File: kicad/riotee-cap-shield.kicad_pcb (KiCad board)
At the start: 2 copper layers, 55.9 x 22.9 mm, 11 parts, among them J1 Conn_01x12, J2 Conn_01x10, SW1 SW_DIP_x08

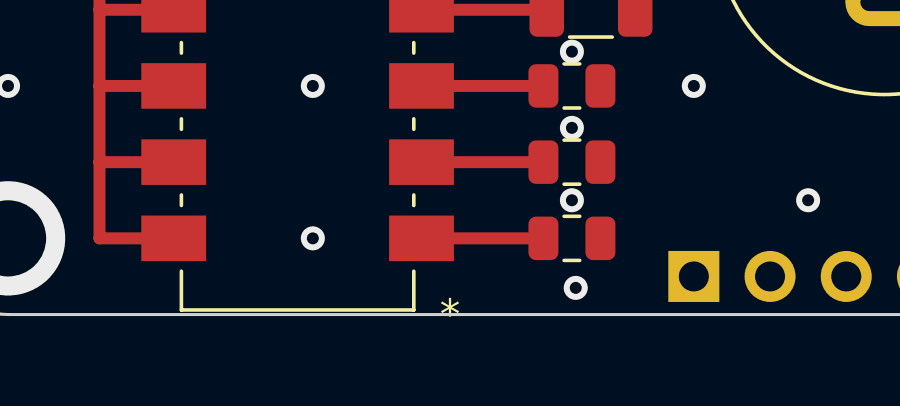
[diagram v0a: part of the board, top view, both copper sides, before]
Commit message: add MPNs in schematics
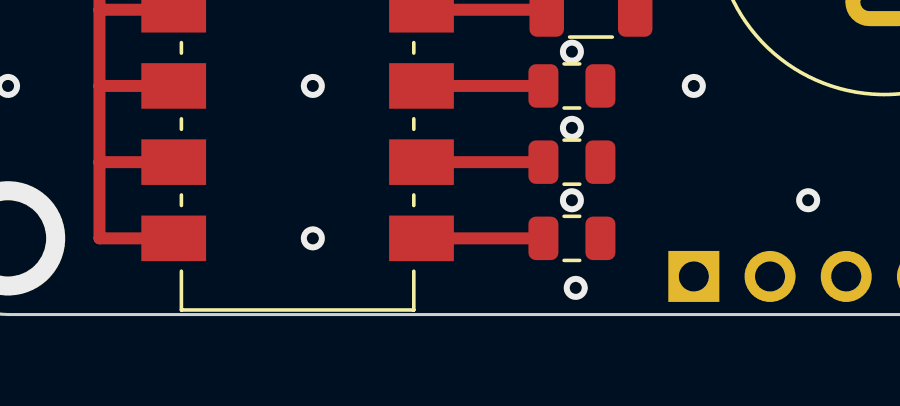
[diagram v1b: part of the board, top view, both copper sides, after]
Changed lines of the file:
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@@
-      (effects (font (size 1 1) (thickness 0.15)))
-    )
-    (fp_text user "*" (at -5.08 -11.43 180) (layer "F.SilkS")
       (effects (font (size 1 1) (thickness 0.15)))
     )

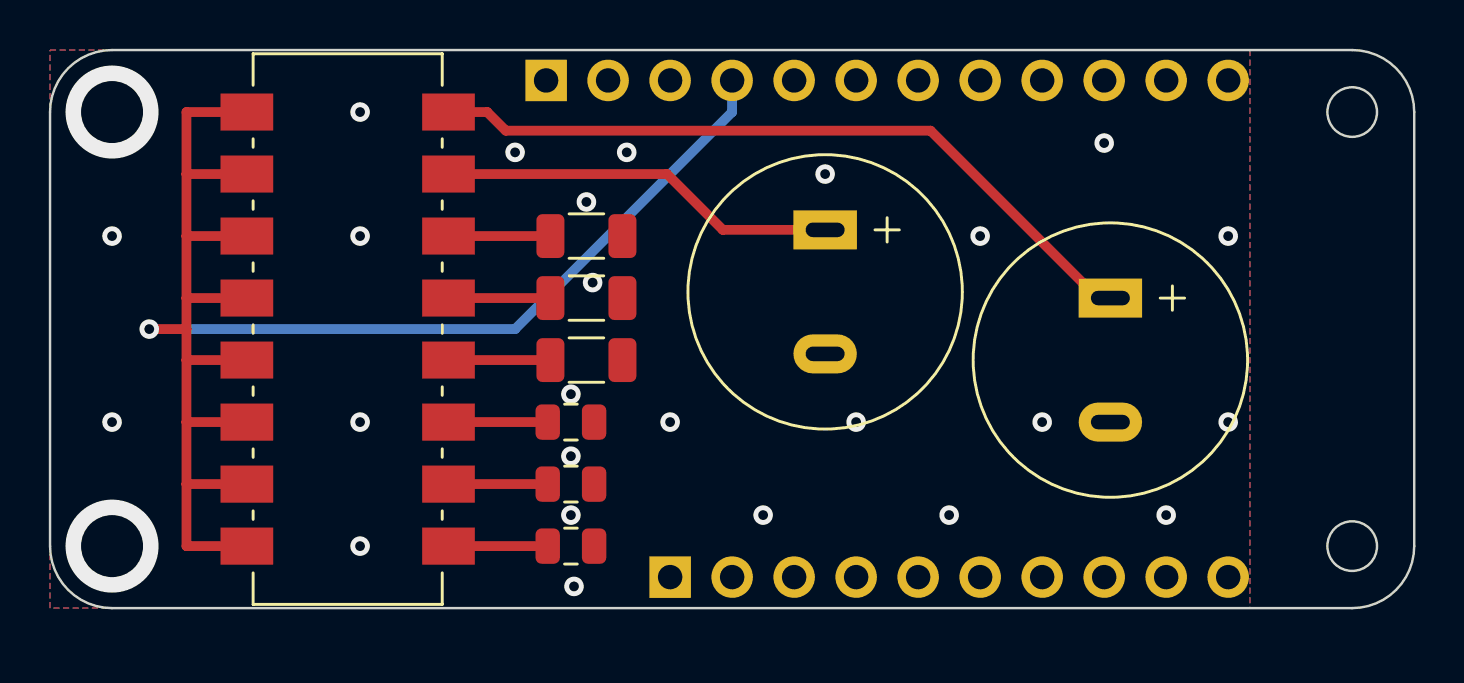
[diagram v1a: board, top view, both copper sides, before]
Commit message: add conformity marks and refine BOM
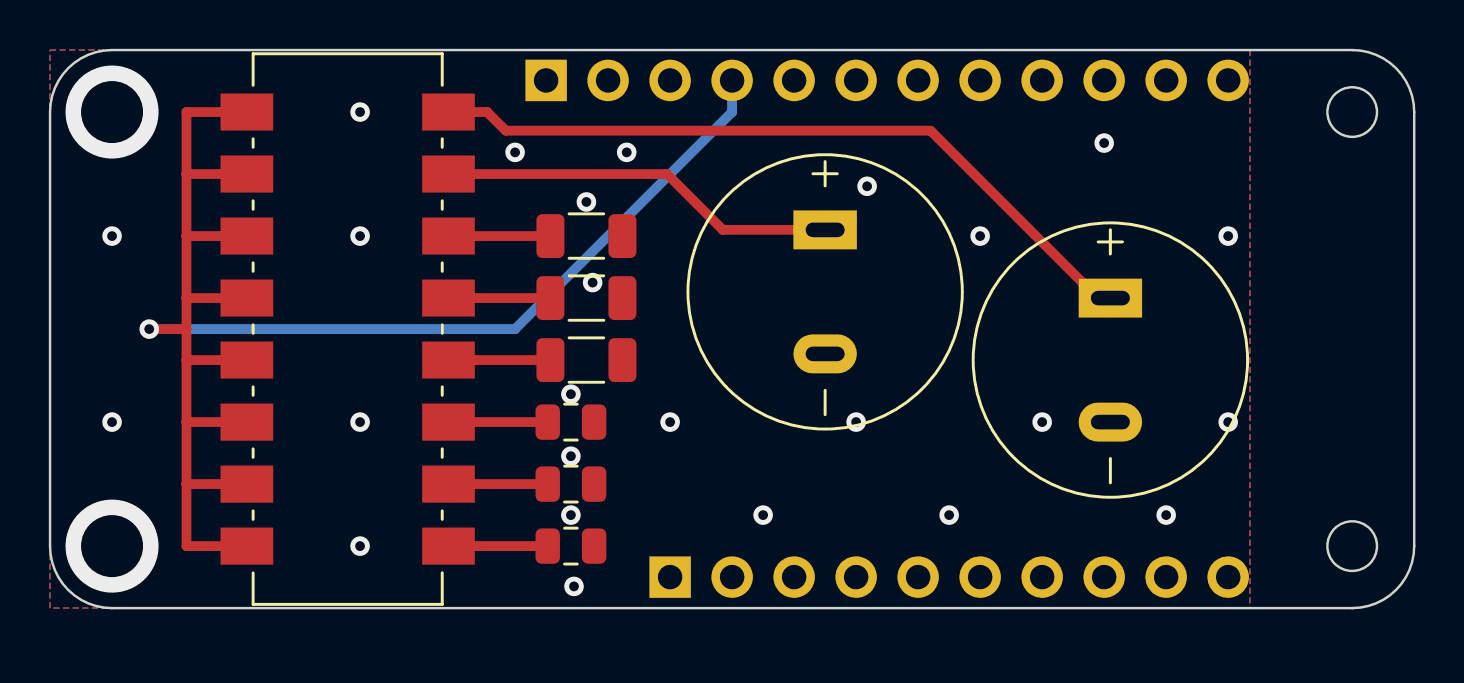
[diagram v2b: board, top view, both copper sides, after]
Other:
- board text added: "Riotee cap shield v1.0"
- board text removed: "Riotee cap shield v0.1"
